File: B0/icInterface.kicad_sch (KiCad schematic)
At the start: 5 parts, among them U001 74HCT00, U002 74HCT125

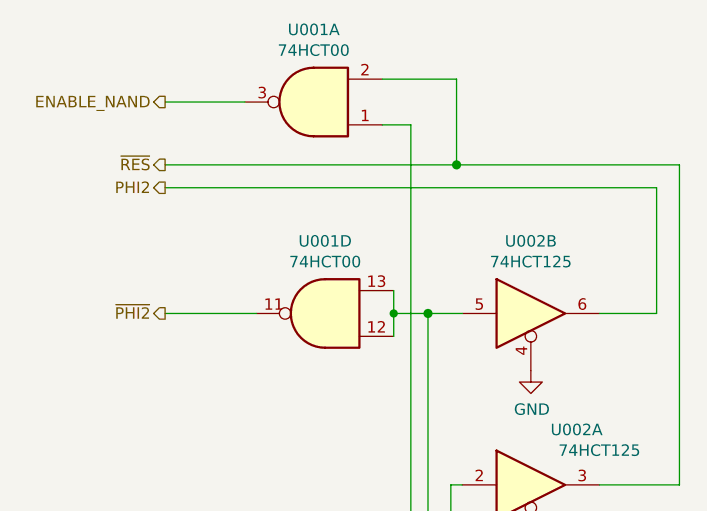
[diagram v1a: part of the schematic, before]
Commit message: B1 CREGA added
Work started on b1. CREGA added.
Minor changes to B0 schematic properties.
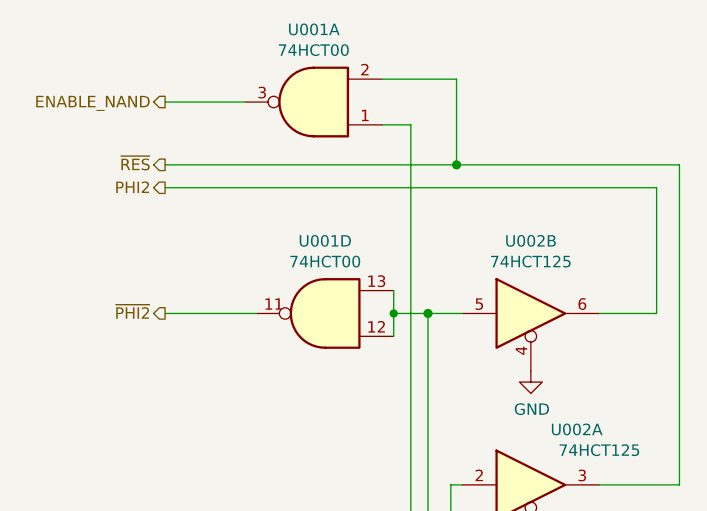
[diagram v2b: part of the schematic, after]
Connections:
- net ~CS renamed ~{CS}
- net ~FLAG renamed ~{FLAG}
- net ~IRQ renamed ~{IRQ}
- net ~PC renamed ~{PC}
- net ~PHI2 renamed ~{PHI2}
- net ~RES renamed ~{RES}
